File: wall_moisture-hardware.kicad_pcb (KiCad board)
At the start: 4 copper layers, 78.5 x 99.3 mm, 46 parts, among them J1 Conn_01x04_Socket, J2 Conn_01x04_Socket, J3 Conn_01x03_Pin, J4 Conn_01x03_Pin, J5 490107670612, Q3 BC847,215, Q4 BSS316N, SW1 DSHP08TSGET, SW2 FSMH, U2 STM32L432KCUx, U3 TPS7A20xxxDBV, U4 TPS7A20xxxDBV, U7 OPA388IDBV, U8 AD7747, Y1 ECS-.327-7-12RR-TR

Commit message: design: Assign LSCS and MPN reference to components
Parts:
- D1: value KT-0805B Blue -> ~
- D2: value KT-0805R Red -> ~
- D3: value KT-0805G Green -> ~
- J1, J2: value Conn_01x04_Socket -> ~
- J3, J4: value Conn_01x03_Pin -> ~
- J5: value 490107670612 -> ~
- Q3: value BC847,215 -> ~
- Q4: value BSS316N -> ~
- SW1: value DSHP08TSGET -> ~
- U2: value STM32L432KCUx -> ~
- U3, U4: value TPS7A20xxxDBV -> ~
- U7: value OPA388IDBV -> ~
- U8: value AD7747 -> ~
- Y1: value ECS-.327-7-12RR-TR -> ~

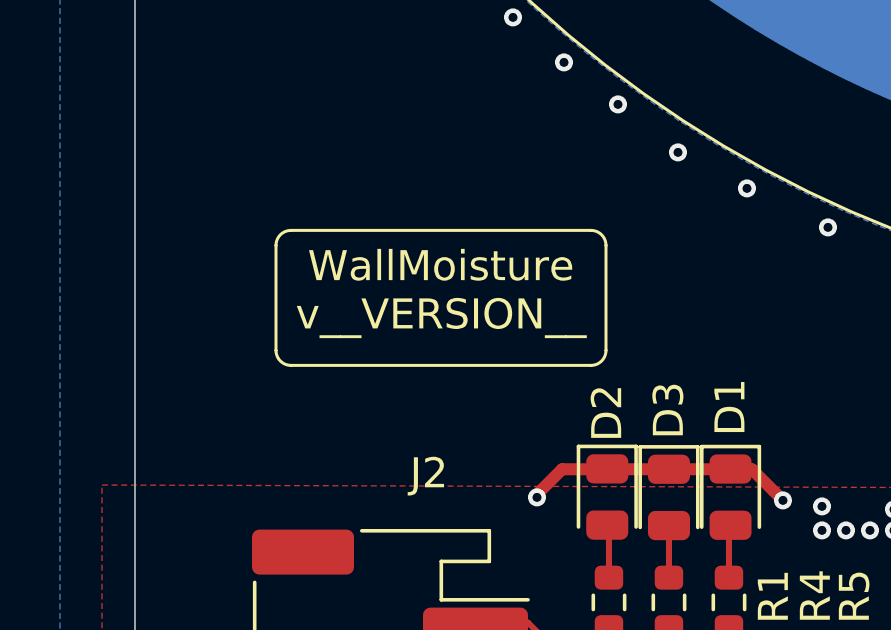
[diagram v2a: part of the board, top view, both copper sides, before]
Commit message: design: Apply the change in schematic sheet name on pcb file
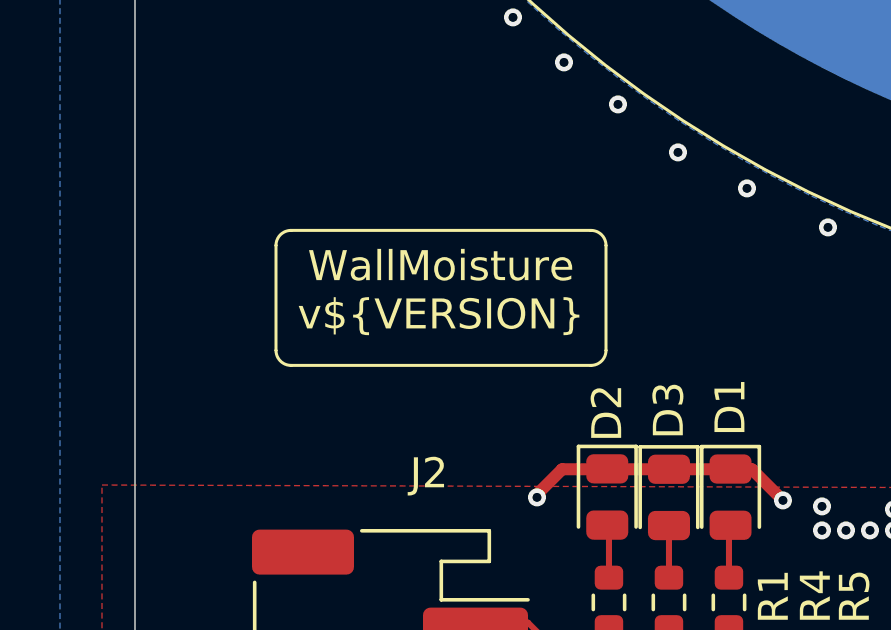
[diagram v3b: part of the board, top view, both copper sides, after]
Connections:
- net /Connector and Power/3.3V renamed /Connectors and Power/3.3V
- net /Connector and Power/MASTER_RX renamed /Connectors and Power/MASTER_RX
- net /Connector and Power/MASTER_TX renamed /Connectors and Power/MASTER_TX
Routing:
- net /Connectors and Power/MASTER_TX: track 91.4 -> 84.2 mm
- net /Connectors and Power/MASTER_RX: track 84.2 -> 91.4 mm
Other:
- board text added: "WallMoisture v${VERSION}"
- board text removed: "WallMoisture v__VERSION__"
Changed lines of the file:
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@@
 	(net 1 "GND")
 	(net 2 "+5V")
-	(net 3 "/Connector and Power/3.3V")
+	(net 3 "/Connectors and Power/3.3V")
 	(net 4 "/Analog frontend/3.3V_LN")
 	(net 5 "Net-(U2-PC15)")
 	(net 6 "Net-(U2-PC14)")
-	(net 7 "/Connector and Power/MASTER_TX")
-	(net 8 "/Connector and Power/MASTER_RX")
+	(net 7 "/Connectors and Power/MASTER_RX")
+	(net 8 "/Connectors and Power/MASTER_TX")
 	(net 9 "/Analog frontend/SENSOR_SHIELD")
 	(net 10 "/µC and digital/TIM1_CH3")
@@
 			(layers "F.Cu" "F.Mask" "F.Paste")
 			(roundrect_rratio 0.25)
-			(net 3 "/Connector and Power/3.3V")
+			(net 3 "/Connectors and Power/3.3V")
 			(pintype "passive")
 		)
@@
 		)
 		(property ki_fp_filters "Connector*:*_1x??_*")
-		(sheetname "/Connector and Power/")
-		(sheetfile "Connector.kicad_sch")
+		(sheetname "/Connectors and Power/")
+		(sheetfile "connectors.kicad_sch")
 		(attr smd)
 		(fp_line
@@
 			(layers "F.Cu" "F.Mask" "F.Paste")
 			(roundrect_rratio 0.25)
-			(net 7 "/Connector and Power/MASTER_TX")
+			(net 8 "/Connectors and Power/MASTER_TX")
 			(pinfunction "Pin_3")
 			(pintype "passive")
@@
 			(layers "F.Cu" "F.Mask" "F.Paste")
 			(roundrect_rratio 0.25)
-			(net 8 "/Connector and Power/MASTER_RX")
+			(net 7 "/Connectors and Power/MASTER_RX")
 			(pinfunction "Pin_4")
 			(pintype "passive")
@@
 		)
 		(property ki_fp_filters "C_*")
-		(sheetname "/Connector and Power/")
-		(sheetfile "Connector.kicad_sch")
+		(sheetname "/Connectors and Power/")
+		(sheetfile "connectors.kicad_sch")
 		(attr smd)
 		(fp_line
@@
 			(layers "F.Cu" "F.Mask" "F.Paste")
 			(roundrect_rratio 0.25)
-			(net 3 "/Connector and Power/3.3V")
+			(net 3 "/Connectors and Power/3.3V")
 			(pintype "passive")
 		)
@@
 		)
 		(property ki_fp_filters "SOT-23-5 *SOT?23?5*")
-		(sheetname "/Connector and Power/")
-		(sheetfile "Connector.kicad_sch")
+		(sheetname "/Connectors and Power/")
+		(sheetfile "connectors.kicad_sch")
 		(attr smd)
 		(fp_line
@@
 			(layers "F.Cu" "F.Mask" "F.Paste")
 			(roundrect_rratio 0.25)
-			(net 3 "/Connector and Power/3.3V")
+			(net 3 "/Connectors and Power/3.3V")
 			(pinfunction "OUT")
 			(pintype "power_out")
@@
 			(layers "F.Cu" "F.Mask" "F.Paste")
 			(roundrect_rratio 0.25)
-			(net 3 "/Connector and Power/3.3V")
+			(net 3 "/Connectors and Power/3.3V")
 			(pinfunction "VDD")
 			(pintype "power_in")
@@
 			(layers "F.Cu" "F.Mask" "F.Paste")
 			(roundrect_rratio 0.25)
-			(net 8 "/Connector and Power/MASTER_RX")
+			(net 7 "/Connectors and Power/MASTER_RX")
 			(pinfunction "PA2")
 			(pintype "bidirectional")
@@
 			(layers "F.Cu" "F.Mask" "F.Paste")
 			(roundrect_rratio 0.25)
-			(net 7 "/Connector and Power/MASTER_TX")
+			(net 8 "/Connectors and Power/MASTER_TX")
 			(pinfunction "PA3")
 			(pintype "bidirectional")
@@
 			(layers "F.Cu" "F.Mask" "F.Paste")
 			(roundrect_rratio 0.25)
-			(net 3 "/Connector and Power/3.3V")
+			(net 3 "/Connectors and Power/3.3V")
 			(pinfunction "VDD")
 			(pintype "power_in")
@@
 			(layers "F.Cu" "F.Mask" "F.Paste")
 			(roundrect_rratio 0.25)
-			(net 3 "/Connector and Power/3.3V")
+			(net 3 "/Connectors and Power/3.3V")
 			(pintype "passive")
 		)
@@
 			)
 		)
-		(property "Description" "Light emitting diode"
+		(property "Description" "Light emitting diode red"
 			(at 0 0 90)
 			(layer "F.Fab")
@@
 			(layers "F.Cu" "F.Mask" "F.Paste")
 			(roundrect_rratio 0.25)
-			(net 3 "/Connector and Power/3.3V")
+			(net 3 "/Connectors and Power/3.3V")
 			(pintype "passive")
 		)
@@
 		)
 		(property ki_fp_filters "C_*")
-		(sheetname "/Connector and Power/")
-		(sheetfile "Connector.kicad_sch")
+		(sheetname "/Connectors and Power/")
+		(sheetfile "connectors.kicad_sch")
 		(attr smd)
 		(fp_line
@@
 		)
 		(property ki_fp_filters "C_*")
-		(sheetname "/Connector and Power/")
-		(sheetfile "Connector.kicad_sch")
+		(sheetname "/Connectors and Power/")
+		(sheetfile "connectors.kicad_sch")
 		(attr smd)
 		(fp_line
@@
 			(layers "F.Cu" "F.Mask" "F.Paste")
 			(roundrect_rratio 0.25)
-			(net 3 "/Connector and Power/3.3V")
+			(net 3 "/Connectors and Power/3.3V")
 			(pintype "passive")
 		)
@@
 		)
 		(property ki_fp_filters "Connector*:*_1x??_*")
-		(sheetname "/Connector and Power/")
-		(sheetfile "Connector.kicad_sch")
+		(sheetname "/Connectors and Power/")
+		(sheetfile "connectors.kicad_sch")
 		(attr smd)
 		(fp_line
@@
 			(layers "F.Cu" "F.Mask" "F.Paste")
 			(roundrect_rratio 0.25)
-			(net 8 "/Connector and Power/MASTER_RX")
+			(net 7 "/Connectors and Power/MASTER_RX")
 			(pinfunction "Pin_1")
 			(pintype "passive")
@@
 			(layers "F.Cu" "F.Mask" "F.Paste")
 			(roundrect_rratio 0.25)
-			(net 7 "/Connector and Power/MASTER_TX")
+			(net 8 "/Connectors and Power/MASTER_TX")
 			(pinfunction "Pin_2")
 			(pintype "passive")
@@
 		)
 		(property ki_fp_filters "SOT-23-5 *SOT?23?5*")
-		(sheetname "/Connector and Power/")
-		(sheetfile "Connector.kicad_sch")
+		(sheetname "/Connectors and Power/")
+		(sheetfile "connectors.kicad_sch")
 		(attr smd)
 		(fp_line
@@
 		)
 		(property ki_fp_filters "C_*")
-		(sheetname "/Connector and Power/")
-		(sheetfile "Connector.kicad_sch")
+		(sheetname "/Connectors and Power/")
+		(sheetfile "connectors.kicad_sch")
 		(attr smd)
 		(fp_line
@@
 			(layers "F.Cu" "F.Mask" "F.Paste")
 			(roundrect_rratio 0.25)
-			(net 3 "/Connector and Power/3.3V")
+			(net 3 "/Connectors and Power/3.3V")
 			(pintype "passive")
 		)
@@
 			(layers "*.Cu" "*.Mask")
 			(remove_unused_layers no)
-			(net 3 "/Connector and Power/3.3V")
+			(net 3 "/Connectors and Power/3.3V")
 			(pinfunction "Pin_2")
 			(pintype "passive")
@@
 		(layer "Edge.Cuts")
 	)
-	(gr_text "WallMoisture\nv__VERSION__"
+	(gr_text "WallMoisture\nv${VERSION}"
 		(at 67.538439 118.027778 0)
 		(layer "F.SilkS")
@@
 	(zone
 		(net 3)
-		(net_name "/Connector and Power/3.3V")
+		(net_name "/Connectors and Power/3.3V")
 		(layer "In1.Cu")
 		(hatch edge 0.5)

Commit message: design: Fix DRC errors
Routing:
- net /Connectors and Power/MASTER_TX: track 84.2 -> 91.4 mm
- net /Connectors and Power/MASTER_RX: track 91.4 -> 84.2 mm
